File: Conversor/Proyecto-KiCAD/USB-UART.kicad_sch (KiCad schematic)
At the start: 30 parts

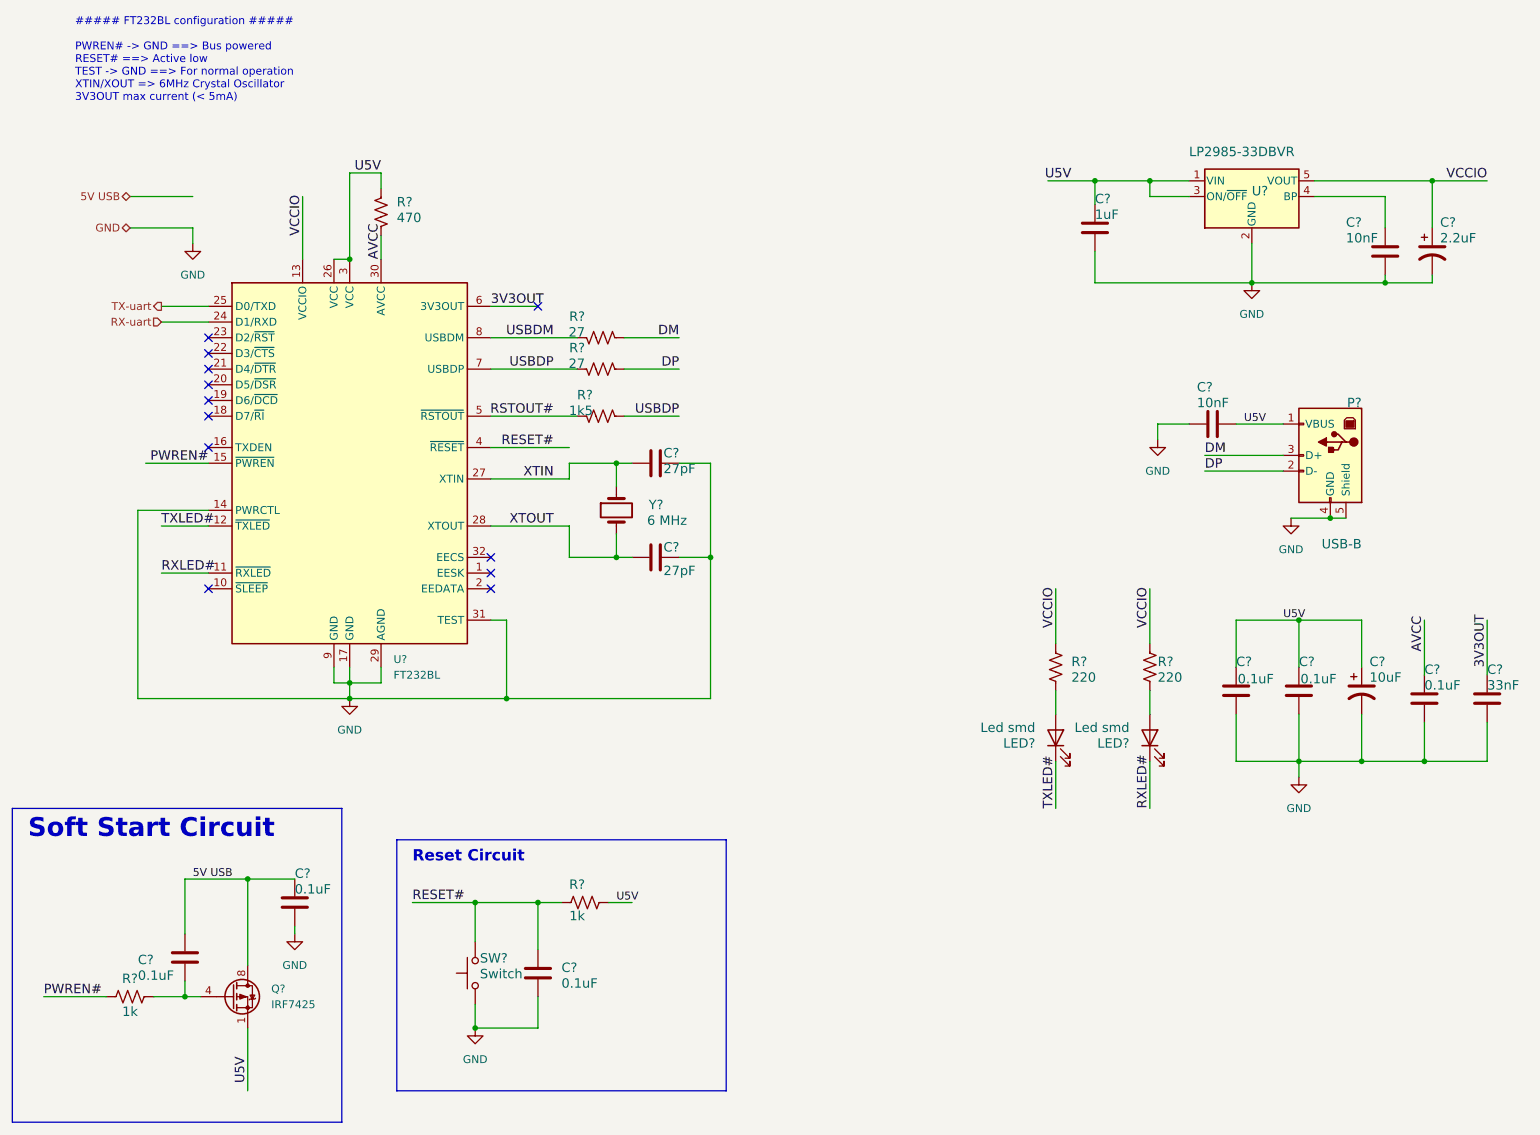
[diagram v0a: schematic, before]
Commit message: Terminar (casi) el traspaso de la placa adaptadora al proyecto
- Queda el selector entre 5V USB y 5V extern, pero todo esta en la hoja
de alimetación general, no dentro de la hoja del DSP
- Cambiar un poco los headers para poder testear (separado en Headers
5V, PWM, ADC, UART, I2C y GPIO)
- Agregar la hoja de datos del LP2985-3.3 (regulador de +3V3)
Por hacer:
  - Ver el tema de la asilacion de las lineas de datos I2C del LM5056,
porque tiene que unirse a una sola linea de datos bidireccional a la
salida del aislador (estan separadas para facilitar la aislación)
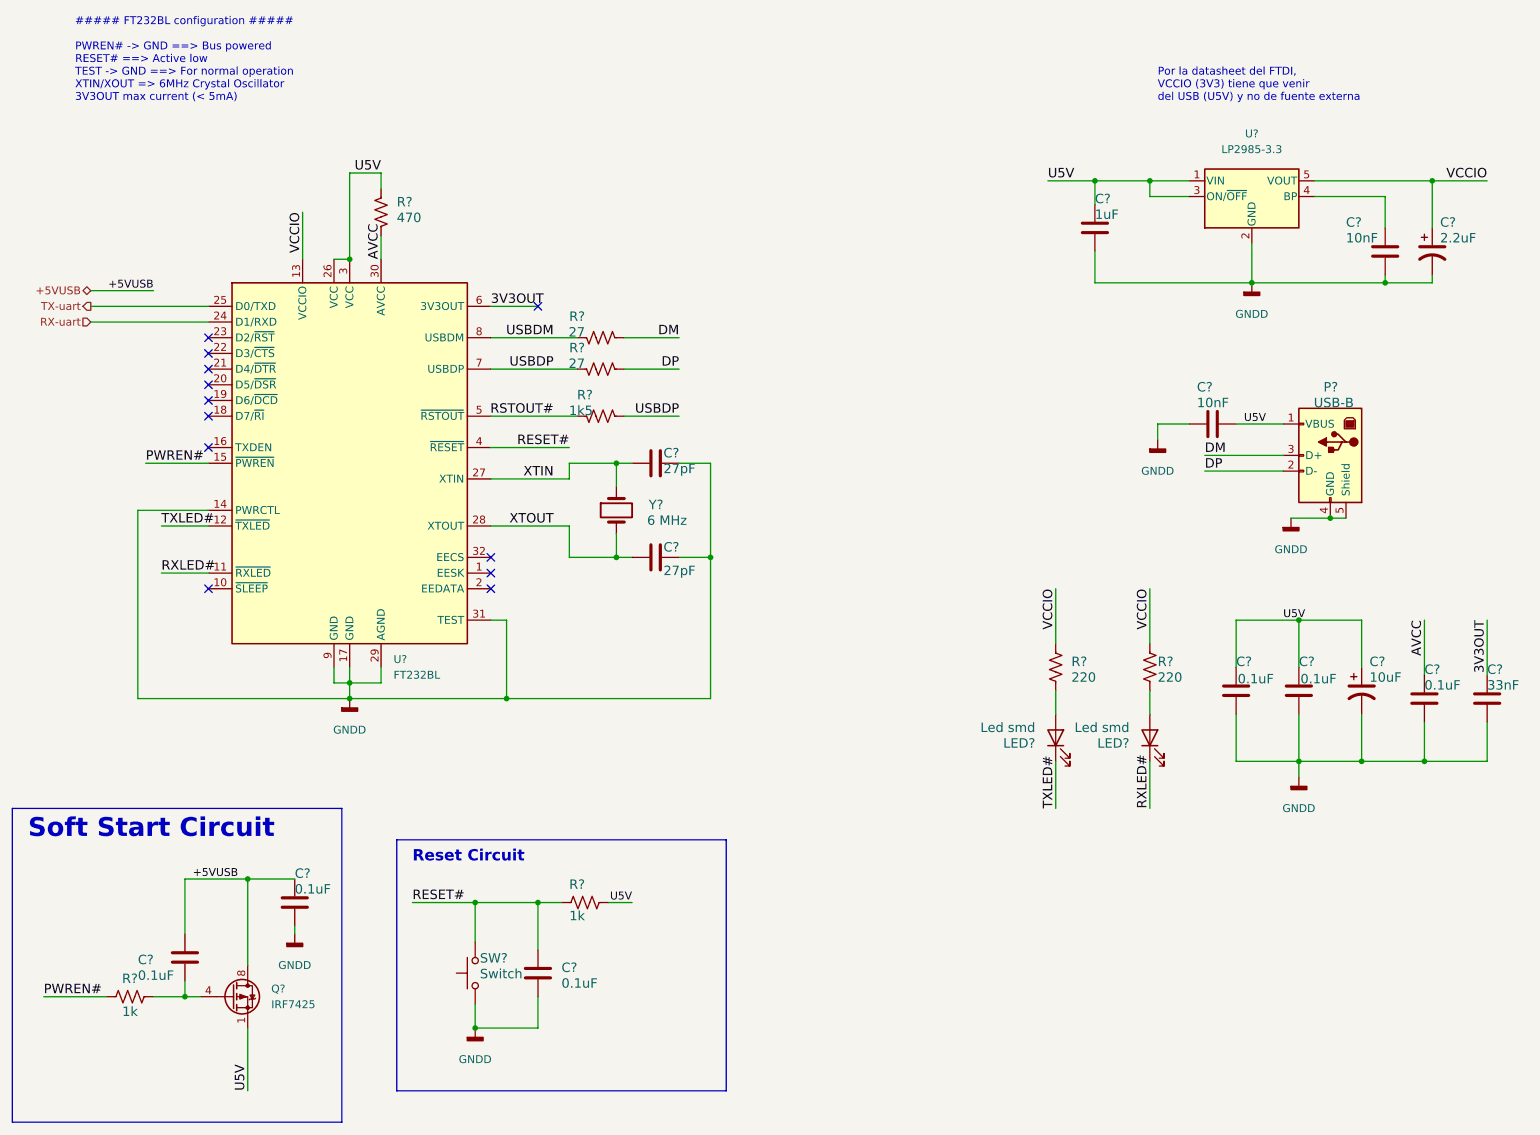
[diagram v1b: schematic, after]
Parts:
- removed U?: LP2985-33DBVR, Package_TO_SOT_SMD:SOT-23-5, symbol Regulator_Linear:LP2985-3.3
- added U?: LP2985-3.3, Package_TO_SOT_SMD:SOT-23-5, symbol Regulator_Linear:LP2985-3.3
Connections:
- net U5V: now also U?.1 (VIN), U?.3 (ON/~{OFF})
- net VCCIO: now also U?.5 (VOUT)
- net at C?.1: now also U?.4 (BP)
- net 5V USB renamed +5VUSB
- net GND renamed GNDD
- net GNDD: now also U?.2 (GND)
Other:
- note added: "Por la datasheet del FTDI, VCCIO (3V3) tiene que venir del USB (U5V) y no de fuente externa"

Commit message: Arreglar todos los errores del ERC
- Agregar flags de 'Not Connected' a pines flotantes
- Agregar resistencias 'falsas' para eliminar los errores de 'Power
input pin not connected to Power output pin'
- Agregar un GND1 conectado a PWR_FLAG para arreglar errores
- Además, agregar bien al proyecto la placa adaptadora importada a KiCad
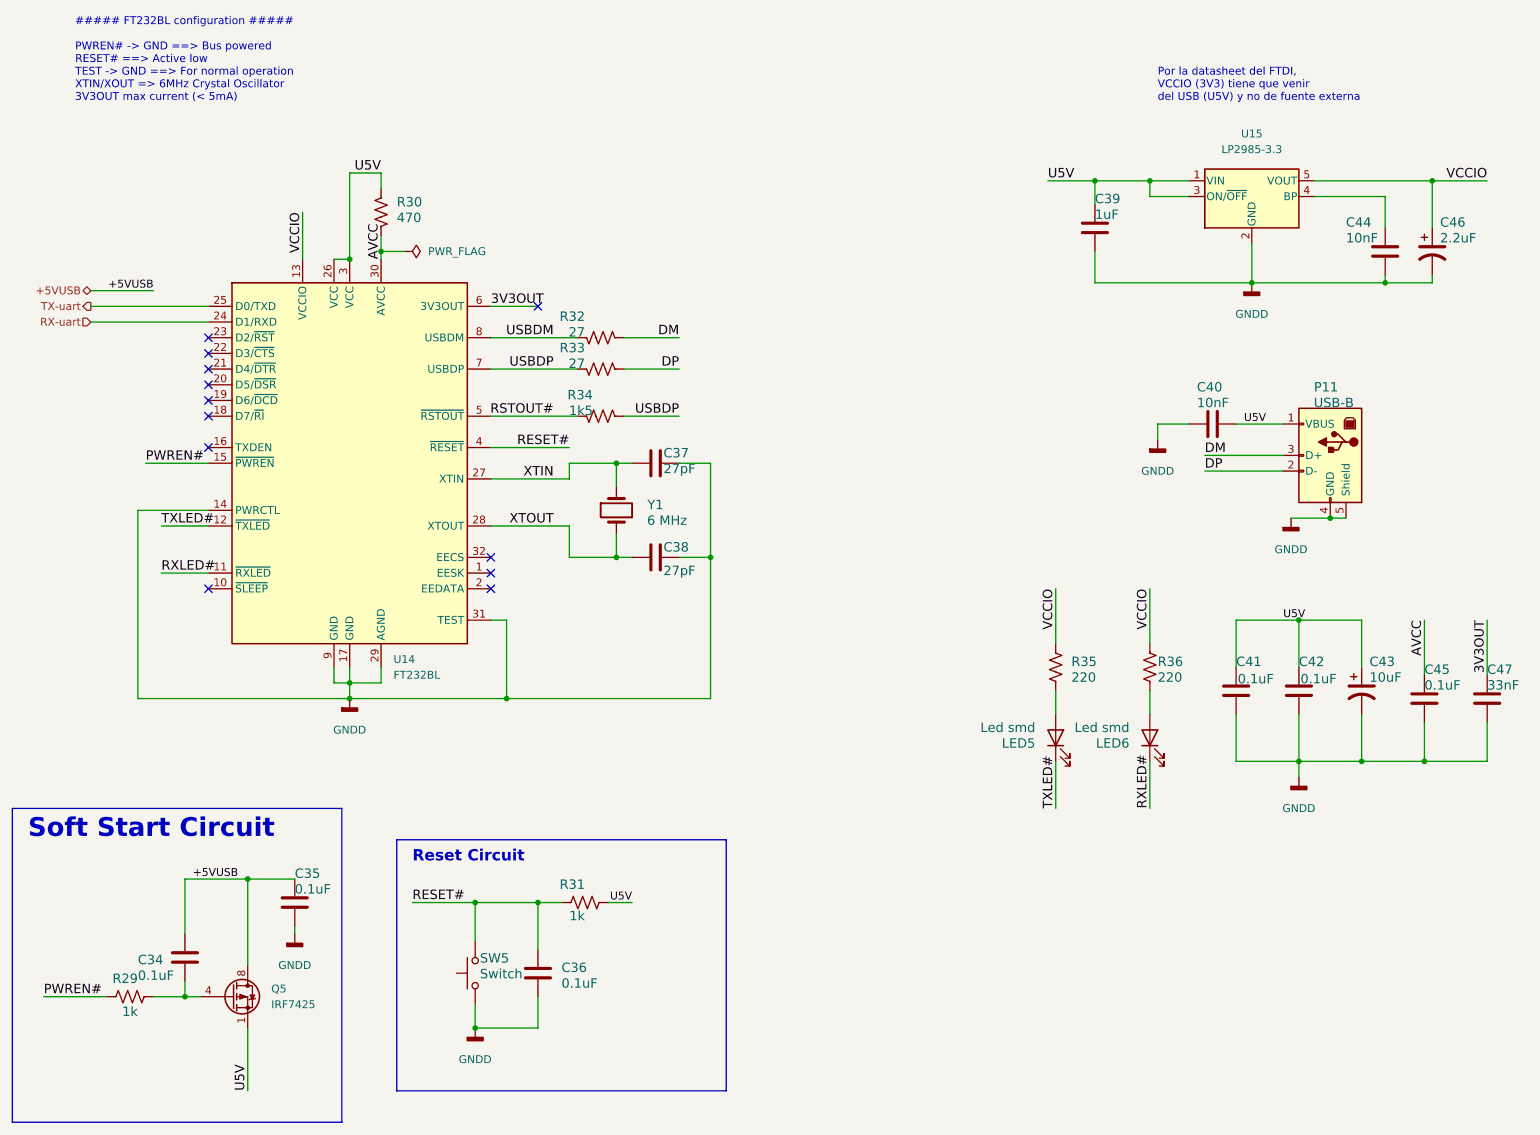
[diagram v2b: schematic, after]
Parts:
- gave numbers to parts that had none: 30
